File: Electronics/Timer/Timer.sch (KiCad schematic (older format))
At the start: 22 parts, among them CN1 RJ12-UNSHLD, U1 MIC5504-3.3YM5, U2 74HC165

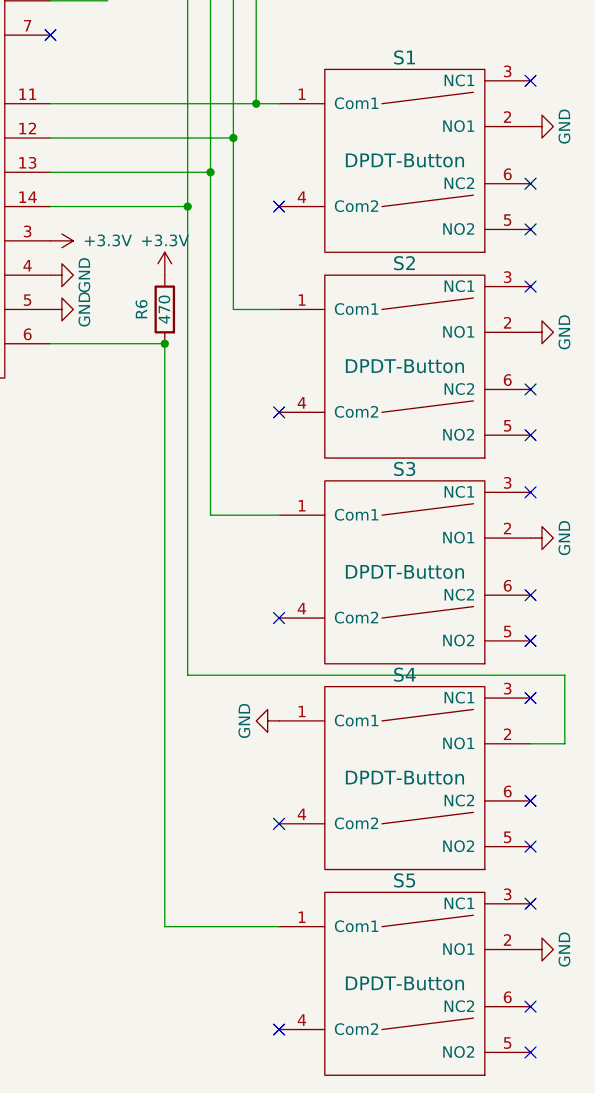
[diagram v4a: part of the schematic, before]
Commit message: Updated trace widths
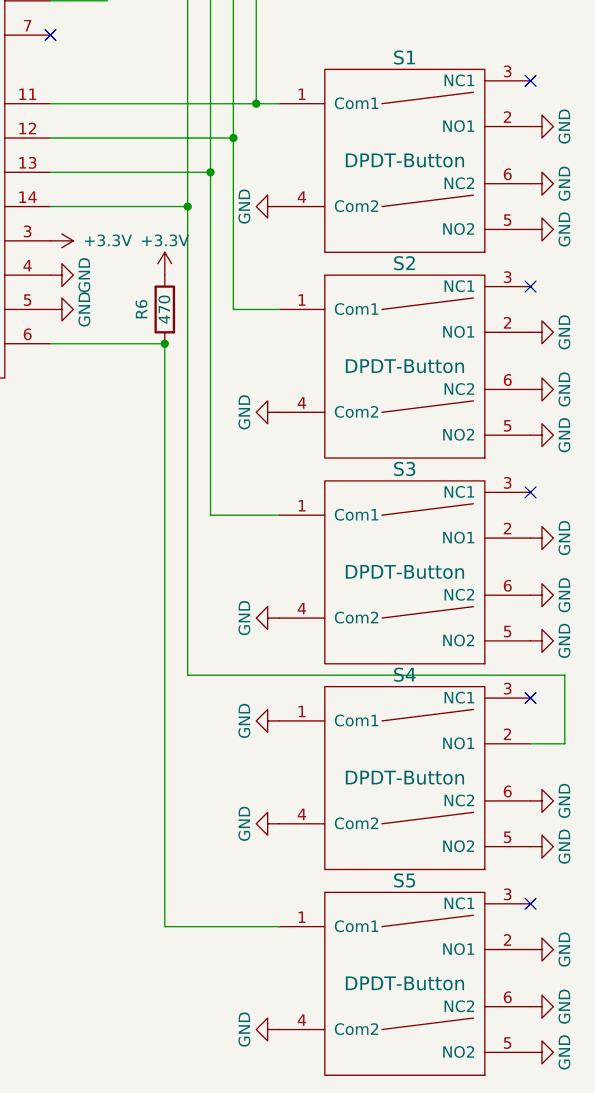
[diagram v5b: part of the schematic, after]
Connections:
- net GND: now also S1.4 (Com2), S1.5 (NO2), S1.6 (NC2), S2.4 (Com2), S2.5 (NO2), S2.6 (NC2), S3.4 (Com2), S3.5 (NO2), S3.6 (NC2), S4.4 (Com2), S4.5 (NO2), S4.6 (NC2), S5.4 (Com2), S5.5 (NO2), S5.6 (NC2)
- no-connect marks 24 -> 9
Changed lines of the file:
@@
 $EndComp
 NoConn ~ 10400 1750
-NoConn ~ 10400 2200
-NoConn ~ 10400 2400
 NoConn ~ 10400 2650
-NoConn ~ 10400 3100
-NoConn ~ 10400 3300
 NoConn ~ 10400 3550
-NoConn ~ 10400 4000
-NoConn ~ 10400 4200
 NoConn ~ 10400 4450
-NoConn ~ 10400 4900
-NoConn ~ 10400 5100
 NoConn ~ 10400 5350
-NoConn ~ 10400 5800
-NoConn ~ 10400 6000
 $Comp
 L power:GND #PWR08
@@
 	0    -1   1    0
 $EndComp
-NoConn ~ 9300 2300
-NoConn ~ 9300 3200
-NoConn ~ 9300 4100
-NoConn ~ 9300 5000
-NoConn ~ 9300 5900
 $Comp
 L Device:R R1
@@
 	10550 4350 8900 4350
 $Comp
-L power:+3.3V #PWR?
+L power:+3.3V #PWR0101
 U 1 1 5B5E304C
 P 8900 900
-F 0 "#PWR?" H 8900 750 50  0001 C CNN
+F 0 "#PWR0101" H 8900 750 50  0001 C CNN
 F 1 "+3.3V" H 8900 1040 50  0000 C CNN
 F 2 "" H 8900 900 50  0001 C CNN
@@
 Wire Wire Line
 	9200 1850 9300 1850
+$Comp
+L power:GND #PWR0102
+U 1 1 5BC0F80F
+P 9300 5000
+F 0 "#PWR0102" H 9300 4750 50  0001 C CNN
+F 1 "GND" H 9300 4850 50  0000 C CNN
+F 2 "" H 9300 5000 50  0001 C CNN
+F 3 "" H 9300 5000 50  0001 C CNN
+	1    9300 5000
+	0    1    -1   0
+$EndComp
+$Comp
+L power:GND #PWR0103
+U 1 1 5BC0F846
+P 9300 5900
+F 0 "#PWR0103" H 9300 5650 50  0001 C CNN
+F 1 "GND" H 9300 5750 50  0000 C CNN
+F 2 "" H 9300 5900 50  0001 C CNN
+F 3 "" H 9300 5900 50  0001 C CNN
+	1    9300 5900
+	0    1    -1   0
+$EndComp
+$Comp
+L power:GND #PWR0104
+U 1 1 5BC0F87D
+P 10400 5100
+F 0 "#PWR0104" H 10400 4850 50  0001 C CNN
+F 1 "GND" H 10400 4950 50  0000 C CNN
+F 2 "" H 10400 5100 50  0001 C CNN
+F 3 "" H 10400 5100 50  0001 C CNN
+	1    10400 5100
+	0    -1   1    0
+$EndComp
+$Comp
+L power:GND #PWR0105
+U 1 1 5BC14F66
+P 10400 4900
+F 0 "#PWR0105" H 10400 4650 50  0001 C CNN
+F 1 "GND" H 10400 4750 50  0000 C CNN
+F 2 "" H 10400 4900 50  0001 C CNN
+F 3 "" H 10400 4900 50  0001 C CNN
+	1    10400 4900
+	0    -1   1    0
+$EndComp
+$Comp
+L power:GND #PWR?
+U 1 1 5BC17578
+P 10400 5800
+F 0 "#PWR?" H 10400 5550 50  0001 C CNN
+F 1 "GND" H 10400 5650 50  0000 C CNN
+F 2 "" H 10400 5800 50  0001 C CNN
+F 3 "" H 10400 5800 50  0001 C CNN
+	1    10400 5800
+	0    -1   1    0
+$EndComp
+$Comp
+L power:GND #PWR?
+U 1 1 5BC175AF
+P 10400 6000
+F 0 "#PWR?" H 10400 5750 50  0001 C CNN
+F 1 "GND" H 10400 5850 50  0000 C CNN
+F 2 "" H 10400 6000 50  0001 C CNN
+F 3 "" H 10400 6000 50  0001 C CNN
+	1    10400 6000
+	0    -1   1    0
+$EndComp
+$Comp
+L power:GND #PWR?
+U 1 1 5BC1AEE3
+P 9300 4100
+F 0 "#PWR?" H 9300 3850 50  0001 C CNN
+F 1 "GND" H 9300 3950 50  0000 C CNN
+F 2 "" H 9300 4100 50  0001 C CNN
+F 3 "" H 9300 4100 50  0001 C CNN
+	1    9300 4100
+	0    1    -1   0
+$EndComp
+$Comp
+L power:GND #PWR?
+U 1 1 5BC1AF1A
+P 10400 4200
+F 0 "#PWR?" H 10400 3950 50  0001 C CNN
+F 1 "GND" H 10400 4050 50  0000 C CNN
+F 2 "" H 10400 4200 50  0001 C CNN
+F 3 "" H 10400 4200 50  0001 C CNN
+	1    10400 4200
+	0    -1   1    0
+$EndComp
+$Comp
+L power:GND #PWR?
+U 1 1 5BC1AF51
+P 10400 4000
+F 0 "#PWR?" H 10400 3750 50  0001 C CNN
+F 1 "GND" H 10400 3850 50  0000 C CNN
+F 2 "" H 10400 4000 50  0001 C CNN
+F 3 "" H 10400 4000 50  0001 C CNN
+	1    10400 4000
+	0    -1   1    0
+$EndComp
+$Comp
+L power:GND #PWR?
+U 1 1 5BC1E4A7
+P 10400 3100
+F 0 "#PWR?" H 10400 2850 50  0001 C CNN
+F 1 "GND" H 10400 2950 50  0000 C CNN
+F 2 "" H 10400 3100 50  0001 C CNN
+F 3 "" H 10400 3100 50  0001 C CNN
+	1    10400 3100
+	0    -1   1    0
+$EndComp
+$Comp
+L power:GND #PWR?
+U 1 1 5BC1E4DE
+P 10400 3300
+F 0 "#PWR?" H 10400 3050 50  0001 C CNN
+F 1 "GND" H 10400 3150 50  0000 C CNN
+F 2 "" H 10400 3300 50  0001 C CNN
+F 3 "" H 10400 3300 50  0001 C CNN
+	1    10400 3300
+	0    -1   1    0
+$EndComp
+$Comp
+L power:GND #PWR?
+U 1 1 5BC1E515
+P 9300 3200
+F 0 "#PWR?" H 9300 2950 50  0001 C CNN
+F 1 "GND" H 9300 3050 50  0000 C CNN
+F 2 "" H 9300 3200 50  0001 C CNN
+F 3 "" H 9300 3200 50  0001 C CNN
+	1    9300 3200
+	0    1    -1   0
+$EndComp
+$Comp
+L power:GND #PWR?
+U 1 1 5BC21A81
+P 9300 2300
+F 0 "#PWR?" H 9300 2050 50  0001 C CNN
+F 1 "GND" H 9300 2150 50  0000 C CNN
+F 2 "" H 9300 2300 50  0001 C CNN
+F 3 "" H 9300 2300 50  0001 C CNN
+	1    9300 2300
+	0    1    -1   0
+$EndComp
+$Comp
+L power:GND #PWR?
+U 1 1 5BC21AB8
+P 10400 2200
+F 0 "#PWR?" H 10400 1950 50  0001 C CNN
+F 1 "GND" H 10400 2050 50  0000 C CNN
+F 2 "" H 10400 2200 50  0001 C CNN
+F 3 "" H 10400 2200 50  0001 C CNN
+	1    10400 2200
+	0    -1   1    0
+$EndComp
+$Comp
+L power:GND #PWR?
+U 1 1 5BC21AEF
+P 10400 2400
+F 0 "#PWR?" H 10400 2150 50  0001 C CNN
+F 1 "GND" H 10400 2250 50  0000 C CNN
+F 2 "" H 10400 2400 50  0001 C CNN
+F 3 "" H 10400 2400 50  0001 C CNN
+	1    10400 2400
+	0    -1   1    0
+$EndComp
 $EndSCHEMATC

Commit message: Updated zener diode footprint and layout
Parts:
- D4: footprint Diodes_SMD:D_SOD-323_HandSoldering -> Diode_SMD:D_SOD-123
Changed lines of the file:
@@
 F 0 "D4" V 6075 3950 50  0000 R CNN
 F 1 "3.3V" V 6325 3950 50  0000 R CNN
-F 2 "Diodes_SMD:D_SOD-323_HandSoldering" H 6200 4000 50  0001 C CNN
+F 2 "Diode_SMD:D_SOD-123" H 6200 4000 50  0001 C CNN
 F 3 "" H 6200 4000 50  0001 C CNN
 	1    6200 4000
@@
 $EndComp
 $Comp
-L power:GND #PWR?
+L power:GND #PWR0106
 U 1 1 5BC17578
 P 10400 5800
-F 0 "#PWR?" H 10400 5550 50  0001 C CNN
+F 0 "#PWR0106" H 10400 5550 50  0001 C CNN
 F 1 "GND" H 10400 5650 50  0000 C CNN
 F 2 "" H 10400 5800 50  0001 C CNN
@@
 $EndComp
 $Comp
-L power:GND #PWR?
+L power:GND #PWR0107
 U 1 1 5BC175AF
 P 10400 6000
-F 0 "#PWR?" H 10400 5750 50  0001 C CNN
+F 0 "#PWR0107" H 10400 5750 50  0001 C CNN
 F 1 "GND" H 10400 5850 50  0000 C CNN
 F 2 "" H 10400 6000 50  0001 C CNN
@@
 $EndComp
 $Comp
-L power:GND #PWR?
+L power:GND #PWR0108
 U 1 1 5BC1AEE3
 P 9300 4100
-F 0 "#PWR?" H 9300 3850 50  0001 C CNN
+F 0 "#PWR0108" H 9300 3850 50  0001 C CNN
 F 1 "GND" H 9300 3950 50  0000 C CNN
 F 2 "" H 9300 4100 50  0001 C CNN
@@
 $EndComp
 $Comp
-L power:GND #PWR?
+L power:GND #PWR0109
 U 1 1 5BC1AF1A
 P 10400 4200
-F 0 "#PWR?" H 10400 3950 50  0001 C CNN
+F 0 "#PWR0109" H 10400 3950 50  0001 C CNN
 F 1 "GND" H 10400 4050 50  0000 C CNN
 F 2 "" H 10400 4200 50  0001 C CNN
@@
 $EndComp
 $Comp
-L power:GND #PWR?
+L power:GND #PWR0110
 U 1 1 5BC1AF51
 P 10400 4000
-F 0 "#PWR?" H 10400 3750 50  0001 C CNN
+F 0 "#PWR0110" H 10400 3750 50  0001 C CNN
 F 1 "GND" H 10400 3850 50  0000 C CNN
 F 2 "" H 10400 4000 50  0001 C CNN
@@
 $EndComp
 $Comp
-L power:GND #PWR?
+L power:GND #PWR0111
 U 1 1 5BC1E4A7
 P 10400 3100
-F 0 "#PWR?" H 10400 2850 50  0001 C CNN
+F 0 "#PWR0111" H 10400 2850 50  0001 C CNN
 F 1 "GND" H 10400 2950 50  0000 C CNN
 F 2 "" H 10400 3100 50  0001 C CNN
@@
 $EndComp
 $Comp
-L power:GND #PWR?
+L power:GND #PWR0112
 U 1 1 5BC1E4DE
 P 10400 3300
-F 0 "#PWR?" H 10400 3050 50  0001 C CNN
+F 0 "#PWR0112" H 10400 3050 50  0001 C CNN
 F 1 "GND" H 10400 3150 50  0000 C CNN
 F 2 "" H 10400 3300 50  0001 C CNN
@@
 $EndComp
 $Comp
-L power:GND #PWR?
+L power:GND #PWR0113
 U 1 1 5BC1E515
 P 9300 3200
-F 0 "#PWR?" H 9300 2950 50  0001 C CNN
+F 0 "#PWR0113" H 9300 2950 50  0001 C CNN
 F 1 "GND" H 9300 3050 50  0000 C CNN
 F 2 "" H 9300 3200 50  0001 C CNN
@@
 $EndComp
 $Comp
-L power:GND #PWR?
+L power:GND #PWR0114
 U 1 1 5BC21A81
 P 9300 2300
-F 0 "#PWR?" H 9300 2050 50  0001 C CNN
+F 0 "#PWR0114" H 9300 2050 50  0001 C CNN
 F 1 "GND" H 9300 2150 50  0000 C CNN
 F 2 "" H 9300 2300 50  0001 C CNN
@@
 $EndComp
 $Comp
-L power:GND #PWR?
+L power:GND #PWR0115
 U 1 1 5BC21AB8
 P 10400 2200
-F 0 "#PWR?" H 10400 1950 50  0001 C CNN
+F 0 "#PWR0115" H 10400 1950 50  0001 C CNN
 F 1 "GND" H 10400 2050 50  0000 C CNN
 F 2 "" H 10400 2200 50  0001 C CNN
@@
 $EndComp
 $Comp
-L power:GND #PWR?
+L power:GND #PWR0116
 U 1 1 5BC21AEF
 P 10400 2400
-F 0 "#PWR?" H 10400 2150 50  0001 C CNN
+F 0 "#PWR0116" H 10400 2150 50  0001 C CNN
 F 1 "GND" H 10400 2250 50  0000 C CNN
 F 2 "" H 10400 2400 50  0001 C CNN

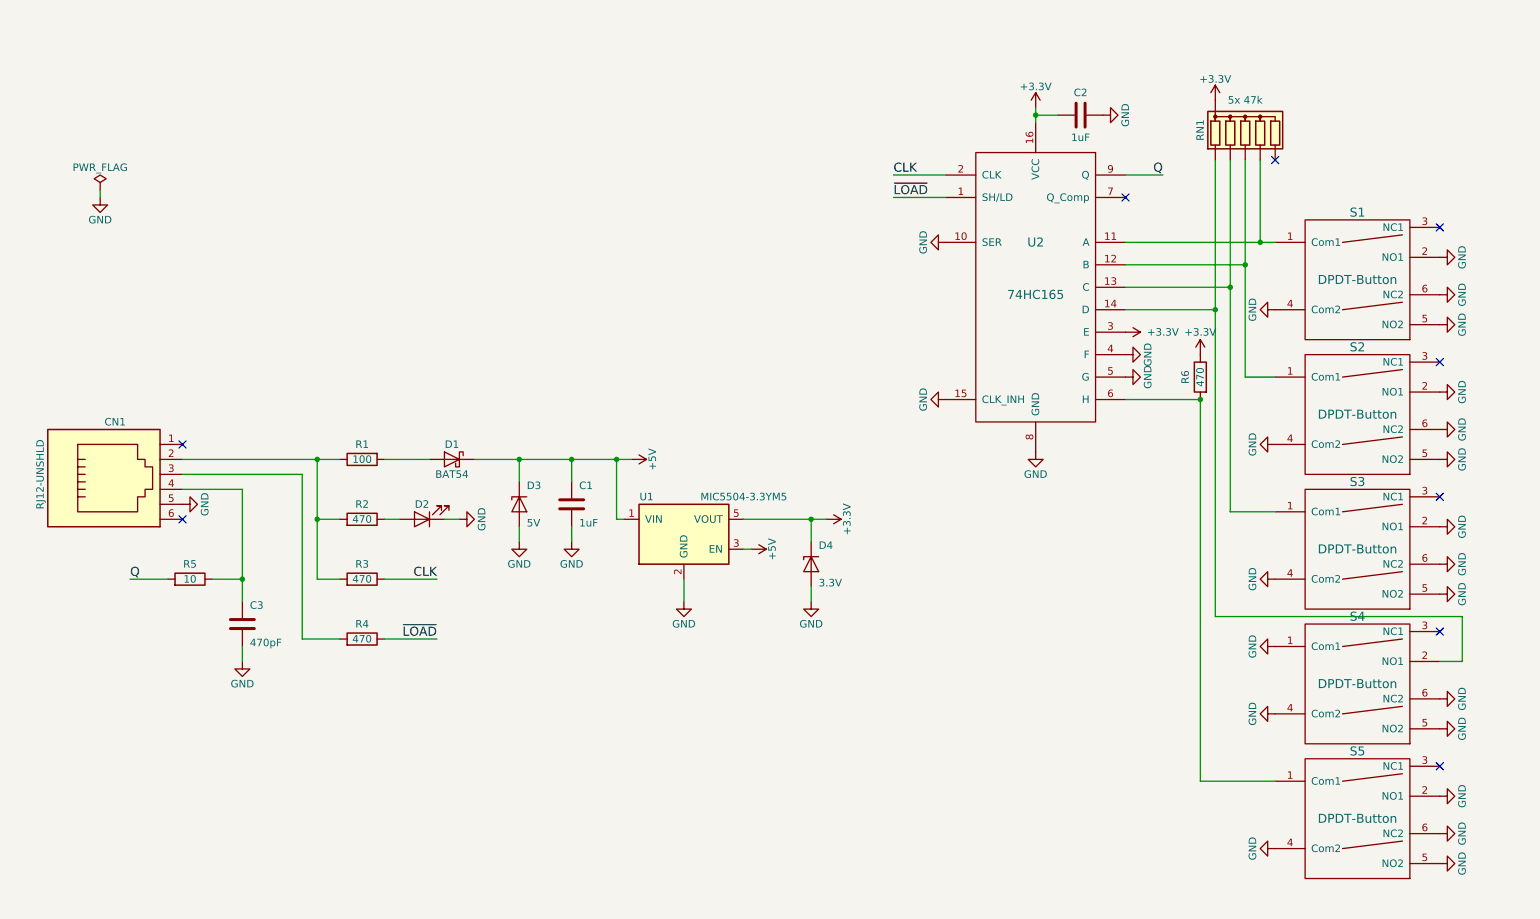
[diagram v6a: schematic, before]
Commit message: Corrected design error in Timer board, updated routing.
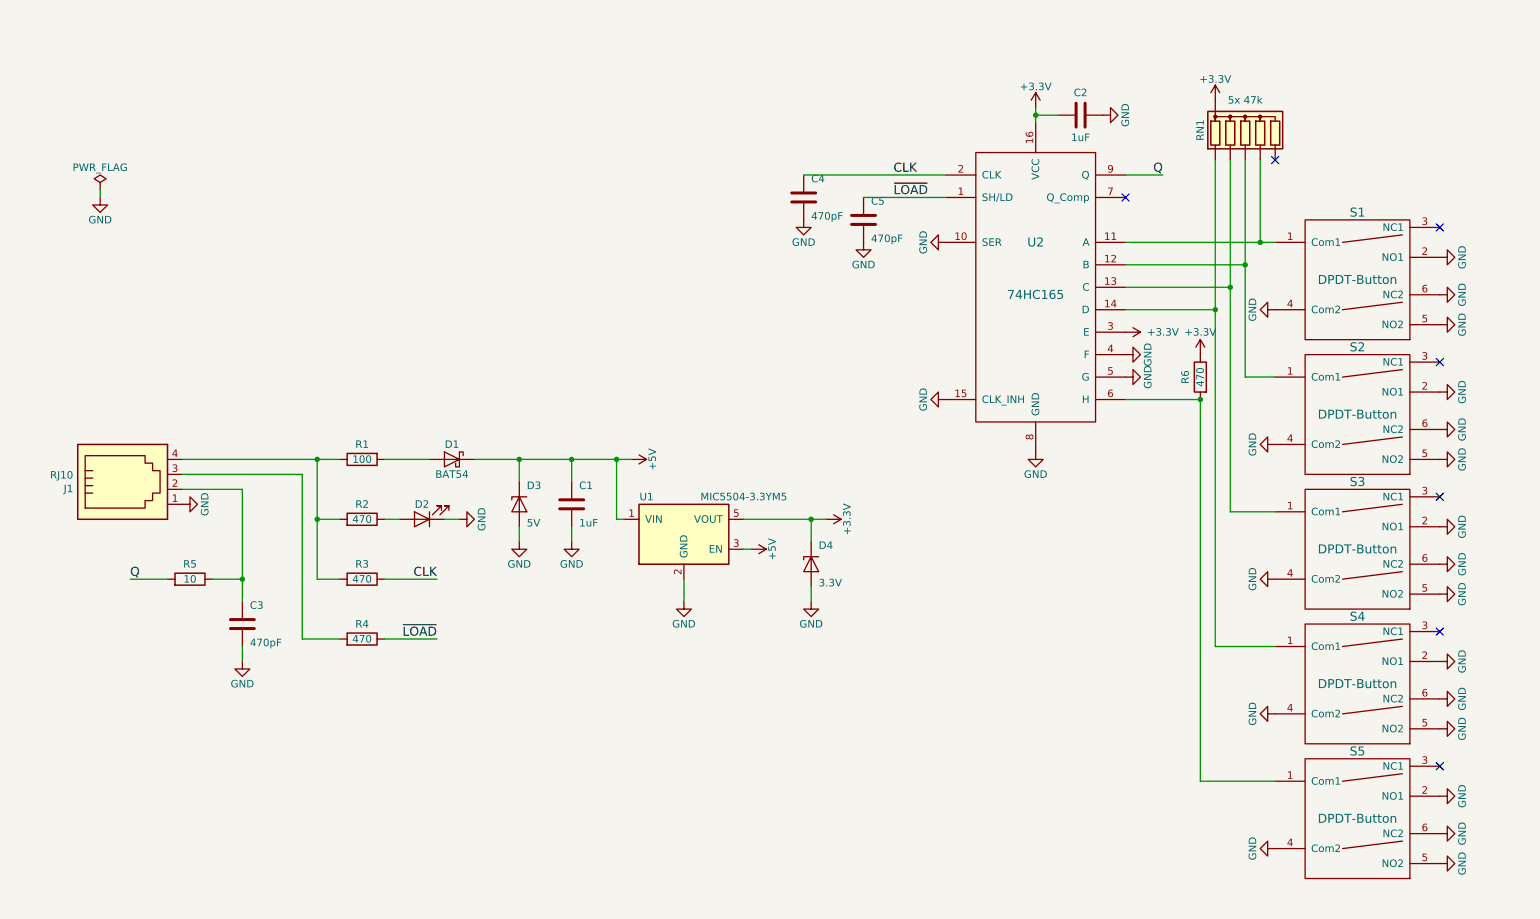
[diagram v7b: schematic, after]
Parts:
- removed CN1: RJ12-UNSHLD, PiKwonDo:TH-RJ12, symbol PiKwonDo:RJ12-UNSHLD
- added C4, C5: 470pF, Capacitor_SMD:C_1206_3216Metric_Pad1.42x1.75mm_HandSolder, symbol Device:C
- added J1: RJ10, Timer:RJ14, symbol Connector:RJ10
- C1, C2, C3: footprint Capacitors_SMD:C_1206_HandSoldering -> Capacitor_SMD:C_1206_3216Metric_Pad1.42x1.75mm_HandSolder
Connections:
- net CLK: now also C4.1
- net GND: now also S4.2 (NO1), C4.2, C5.2, J1.1; no longer S4.1 (Com1)
- net ~LOAD~: now also C5.1
- net at RN1.2 (R1), U2.14 (D): now also S4.1 (Com1); no longer S4.2 (NO1)
- net at R1.1, R2.2, R3.2: now also J1.4
- net at R4.2: now also J1.3
- net at C3.1, R5.1: now also J1.2
- no-connect marks 9 -> 7
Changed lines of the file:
@@
 $EndComp
-$Comp
-L PiKwonDo:RJ12-UNSHLD CN1
-U 1 1 5B2D8F12
-P 1550 3400
-F 0 "CN1" V 1200 3400 50  0000 C CNN
-F 1 "RJ12-UNSHLD" H 1550 3900 50  0000 C CNN
-F 2 "PiKwonDo:TH-RJ12" H 1550 3400 50  0001 C CNN
-F 3 "" H 1550 3400 50  0001 C CNN
-	1    1550 3400
-	0    -1   1    0
-$EndComp
-NoConn ~ 2000 3700
-NoConn ~ 2000 3200
 $Comp
 L Device:LED D2
@@
 F 0 "C2" V 8150 1000 50  0000 C CNN
 F 1 "1uF" V 7850 1000 50  0000 C CNN
-F 2 "Capacitors_SMD:C_1206_HandSoldering" H 8038 850 50  0001 C CNN
+F 2 "Capacitor_SMD:C_1206_3216Metric_Pad1.42x1.75mm_HandSolder" H 8038 850 50  0001 C CNN
 F 3 "" H 8000 1000 50  0001 C CNN
 	1    8000 1000
@@
 F 0 "C1" H 4550 3725 50  0000 R CNN
 F 1 "1uF" H 4550 3475 50  0000 R CNN
-F 2 "Capacitors_SMD:C_1206_HandSoldering" H 4638 3450 50  0001 C CNN
+F 2 "Capacitor_SMD:C_1206_3216Metric_Pad1.42x1.75mm_HandSolder" H 4638 3450 50  0001 C CNN
 F 3 "" H 4600 3600 50  0001 C CNN
 	1    4600 3600
@@
 F 0 "C3" H 2350 4525 50  0000 R CNN
 F 1 "470pF" H 2350 4275 50  0000 R CNN
-F 2 "Capacitors_SMD:C_1206_HandSoldering" H 2438 4250 50  0001 C CNN
+F 2 "Capacitor_SMD:C_1206_3216Metric_Pad1.42x1.75mm_HandSolder" H 2438 4250 50  0001 C CNN
 F 3 "" H 2400 4400 50  0001 C CNN
 	1    2400 4400
@@
 L power:GND #PWR023
 U 1 1 5B5EA5B2
-P 9300 4550
-F 0 "#PWR023" H 9300 4300 50  0001 C CNN
-F 1 "GND" H 9300 4400 50  0000 C CNN
-F 2 "" H 9300 4550 50  0001 C CNN
-F 3 "" H 9300 4550 50  0001 C CNN
-	1    9300 4550
-	0    1    -1   0
+P 10400 4650
+F 0 "#PWR023" H 10400 4400 50  0001 C CNN
+F 1 "GND" H 10400 4500 50  0000 C CNN
+F 2 "" H 10400 4650 50  0001 C CNN
+F 3 "" H 10400 4650 50  0001 C CNN
+	1    10400 4650
+	0    -1   1    0
 $EndComp
 $Comp
@@
 	8300 1400 8550 1400
 Wire Wire Line
-	7100 1400 6750 1400
-Wire Wire Line
-	7100 1550 6750 1550
-Wire Wire Line
 	8300 1850 9200 1850
 Connection ~ 9100 2000
@@
 $EndComp
 Wire Wire Line
-	10400 4650 10550 4650
-Wire Wire Line
-	10550 4650 10550 4350
-Wire Wire Line
-	10550 4350 8900 4350
+	9300 4550 8900 4550
 $Comp
 L power:+3.3V #PWR0101
@@
 	9000 2150 9000 3650
 Wire Wire Line
-	8900 2300 8900 4350
+	8900 2300 8900 4550
 Wire Wire Line
 	9200 1850 9300 1850
@@
 	0    -1   1    0
 $EndComp
+$Comp
+L Device:C C4
+U 1 1 5C3BCA70
+P 6150 1550
+F 0 "C4" H 6100 1675 50  0000 R CNN
+F 1 "470pF" H 6100 1425 50  0000 R CNN
+F 2 "Capacitor_SMD:C_1206_3216Metric_Pad1.42x1.75mm_HandSolder" H 6188 1400 50  0001 C CNN
+F 3 "" H 6150 1550 50  0001 C CNN
+	1    6150 1550
+	-1   0    0    -1
+$EndComp
+Wire Wire Line
+	6150 1400 7100 1400
+$Comp
+L power:GND #PWR0117
+U 1 1 5C3BDD23
+P 6150 1700
+F 0 "#PWR0117" H 6150 1450 50  0001 C CNN
+F 1 "GND" H 6150 1550 50  0000 C CNN
+F 2 "" H 6150 1700 50  0001 C CNN
+F 3 "" H 6150 1700 50  0001 C CNN
+	1    6150 1700
+	-1   0    0    -1
+$EndComp
+$Comp
+L Device:C C5
+U 1 1 5C3C02A8
+P 6550 1700
+F 0 "C5" H 6500 1825 50  0000 R CNN
+F 1 "470pF" H 6500 1575 50  0000 R CNN
+F 2 "Capacitor_SMD:C_1206_3216Metric_Pad1.42x1.75mm_HandSolder" H 6588 1550 50  0001 C CNN
+F 3 "" H 6550 1700 50  0001 C CNN
+	1    6550 1700
+	-1   0    0    -1
+$EndComp
+$Comp
+L power:GND #PWR0118
+U 1 1 5C3C02AF
+P 6550 1850
+F 0 "#PWR0118" H 6550 1600 50  0001 C CNN
+F 1 "GND" H 6550 1700 50  0000 C CNN
+F 2 "" H 6550 1850 50  0001 C CNN
+F 3 "" H 6550 1850 50  0001 C CNN
+	1    6550 1850
+	-1   0    0    -1
+$EndComp
+Wire Wire Line
+	6550 1550 7100 1550
+$Comp
+L Connector:RJ10 J1
+U 1 1 5C3D5B2C
+P 1600 3500
+F 0 "J1" H 1270 3504 50  0000 R CNN
+F 1 "RJ10" H 1270 3595 50  0000 R CNN
+F 2 "Timer:RJ14" V 1600 3550 50  0001 C CNN
+F 3 "~" V 1600 3550 50  0001 C CNN
+	1    1600 3500
+	1    0    0    -1
+$EndComp
 $EndSCHEMATC
